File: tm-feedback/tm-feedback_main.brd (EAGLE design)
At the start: 100 x 80 mm, 24 parts

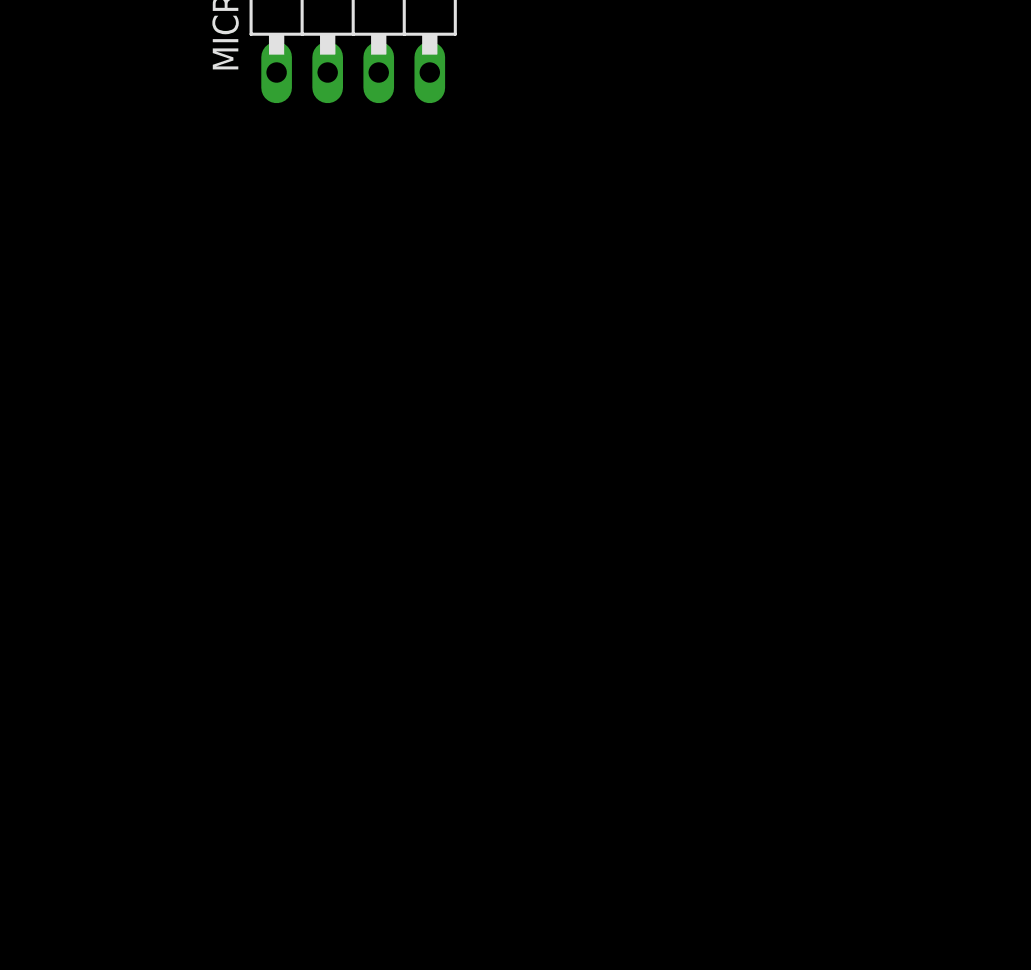
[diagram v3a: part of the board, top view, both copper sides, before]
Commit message: Add some custom library components to schematics
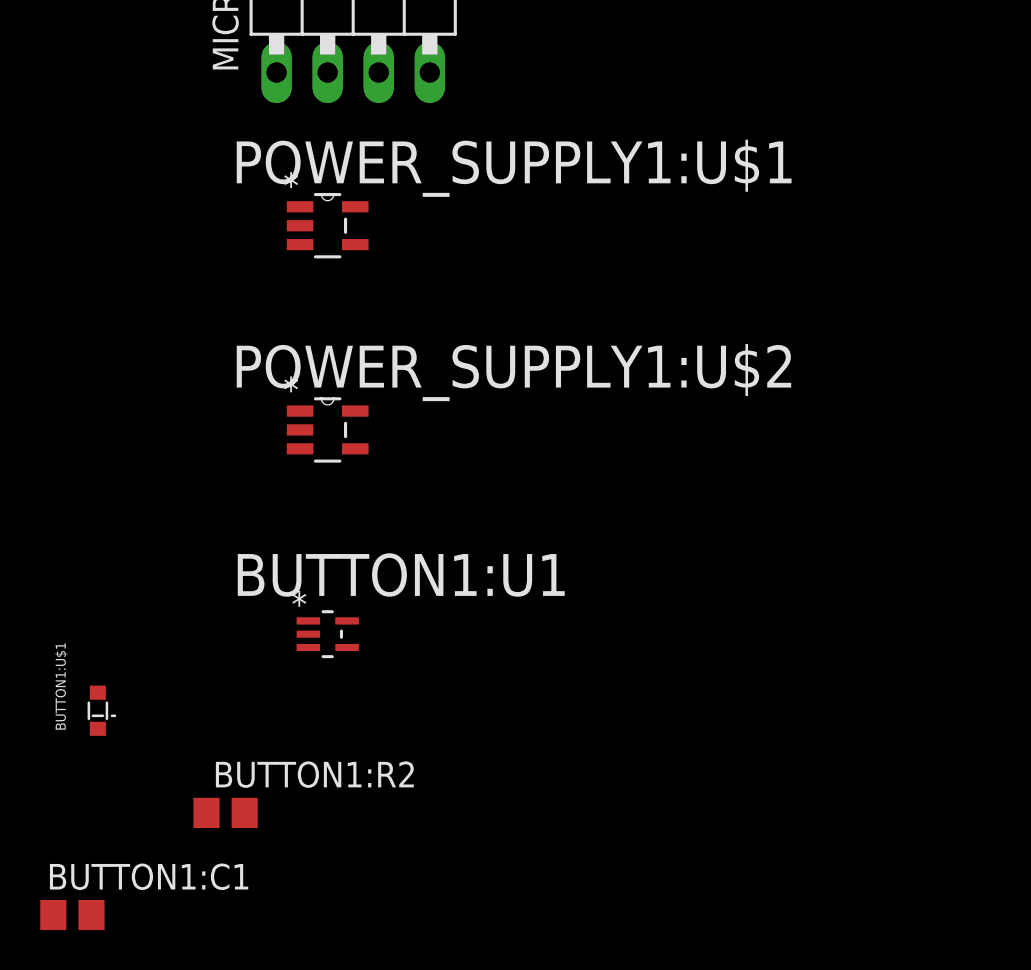
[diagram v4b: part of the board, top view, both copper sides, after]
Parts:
- added BUTTON1:C1: (no value), rcl:C0805
- added BUTTON1:R2: (no value), resistor:R0805
- added BUTTON1:U$1: DB2S308, tactile-music:SOD-523
- added BUTTON1:U1: 74AUP1G17GW, tactile-music:SOT65P212X110-5N
- added POWER_SUPPLY1:U$1, POWER_SUPPLY1:U$2: MCP1824T-3302E/OT, tactile-music:SOT95P270X145-5N
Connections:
- new net BUTTON1:VCC: BUTTON1:U1.5
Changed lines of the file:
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@@
 <element name="MICROCONTROLLER1:JP1" library="pinhead" package="1X06/90" value="" x="-54.61" y="-114.3"/>
 <element name="MICROCONTROLLER1:JP2" library="pinhead" package="1X04/90" value="" x="-57.15" y="-128.27"/>
+<element name="POWER_SUPPLY1:U$1" library="tactile-music" package="SOT95P270X145-5N" value="MCP1824T-3302E/OT" x="-58.42" y="-139.7">
+<attribute name="MPN" value="MCP1824T-3302E/OT" x="-58.42" y="-139.7" size="1.778" layer="27" display="off"/>
+<attribute name="SUPPLIER" value="Microchip" x="-58.42" y="-139.7" size="1.778" layer="27" display="off"/>
+<attribute name="OC_NEWARK" value="40M0704" x="-58.42" y="-139.7" size="1.778" layer="27" display="off"/>
+<attribute name="PACKAGE" value="SOT23-5" x="-58.42" y="-139.7" size="1.778" layer="27" display="off"/>
+<attribute name="OC_FARNELL" value="1578387" x="-58.42" y="-139.7" size="1.778" layer="27" display="off"/>
+</element>
+<element name="POWER_SUPPLY1:U$2" library="tactile-music" package="SOT95P270X145-5N" value="MCP1824T-3302E/OT" x="-58.42" y="-149.86">
+<attribute name="MPN" value="MCP1824T-3302E/OT" x="-58.42" y="-149.86" size="1.778" layer="27" display="off"/>
+<attribute name="SUPPLIER" value="Microchip" x="-58.42" y="-149.86" size="1.778" layer="27" display="off"/>
+<attribute name="OC_NEWARK" value="40M0704" x="-58.42" y="-149.86" size="1.778" layer="27" display="off"/>
+<attribute name="PACKAGE" value="SOT23-5" x="-58.42" y="-149.86" size="1.778" layer="27" display="off"/>
+<attribute name="OC_FARNELL" value="1578387" x="-58.42" y="-149.86" size="1.778" layer="27" display="off"/>
+</element>
+<element name="BUTTON1:U1" library="tactile-music" package="SOT65P212X110-5N" value="74AUP1G17GW" x="-58.42" y="-160.02">
+<attribute name="MPN" value="74AUP1G17GW " x="-58.42" y="-160.02" size="1.778" layer="27" display="off"/>
+<attribute name="SUPPLIER" value="NXP " x="-58.42" y="-160.02" size="1.778" layer="27" display="off"/>
+<attribute name="OC_NEWARK" value="55W4625 " x="-58.42" y="-160.02" size="1.778" layer="27" display="off"/>
+<attribute name="PACKAGE" value="TSSOP-5" x="-58.42" y="-160.02" size="1.778" layer="27" display="off"/>
+<attribute name="OC_FARNELL" value="2164682 " x="-58.42" y="-160.02" size="1.778" layer="27" display="off"/>
+</element>
+<element name="BUTTON1:R2" library="resistor" package="R0805" value="" x="-63.5" y="-168.91"/>
+<element name="BUTTON1:U$1" library="tactile-music" package="SOD-523" value="DB2S308" x="-69.85" y="-163.83"/>
+<element name="BUTTON1:C1" library="rcl" package="C0805" value="" x="-71.12" y="-173.99"/>
 </elements>
 <signals>
@@
 <wire x1="6.13" y1="-40.02" x2="3.49" y2="-53.34" width="0" layer="19" extent="1-1"/>
 </signal>
+<signal name="BUTTON1:VCC">
+<contactref element="BUTTON1:U1" pad="5"/>
+</signal>
 </signals>

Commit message: Made a start on the bluetooth module
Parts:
- added BLUETOOTH1:C1: (no value), rcl:C0805
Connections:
- removed net BLUETOOTH1:VDD: BLUETOOTH1:U$1.23
- new net D_3V3: BLUETOOTH1:C1.1, BLUETOOTH1:U$1.23
- net D_GND: now also BLUETOOTH1:C1.2
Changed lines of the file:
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@@
 <element name="BUTTON1:U$1" library="tactile-music" package="SOD-523" value="DB2S308" x="-69.85" y="-163.83"/>
 <element name="BUTTON1:C1" library="rcl" package="C0805" value="" x="-71.12" y="-173.99"/>
+<element name="BLUETOOTH1:C1" library="rcl" package="C0805" value="" x="-71.12" y="-179.07"/>
 </elements>
 <signals>
-<signal name="BLUETOOTH1:VDD">
-<contactref element="BLUETOOTH1:U$1" pad="23"/>
-</signal>
 <signal name="D_GND">
 <contactref element="BLUETOOTH1:U$1" pad="9"/>
 <contactref element="BLUETOOTH1:U$1" pad="16"/>
 <contactref element="BLUETOOTH1:U$1" pad="1"/>
+<contactref element="BLUETOOTH1:C1" pad="2"/>
 <contactref element="BLUETOOTH1:U$1" pad="24"/>
+<wire x1="1.87" y1="-21.18" x2="-70.17" y2="-179.07" width="0" layer="19" extent="1-1"/>
 <wire x1="1.87" y1="-10.28" x2="1.87" y2="-21.18" width="0" layer="19" extent="1-1"/>
 <wire x1="13.37" y1="-21.18" x2="1.87" y2="-21.18" width="0" layer="19" extent="1-1"/>
@@
 <contactref element="BUTTON1:U1" pad="5"/>
 </signal>
+<signal name="D_3V3">
+<contactref element="BLUETOOTH1:U$1" pad="23"/>
+<contactref element="BLUETOOTH1:C1" pad="1"/>
+<wire x1="13.37" y1="-11.48" x2="-72.07" y2="-179.07" width="0" layer="19" extent="1-1"/>
+</signal>
 </signals>

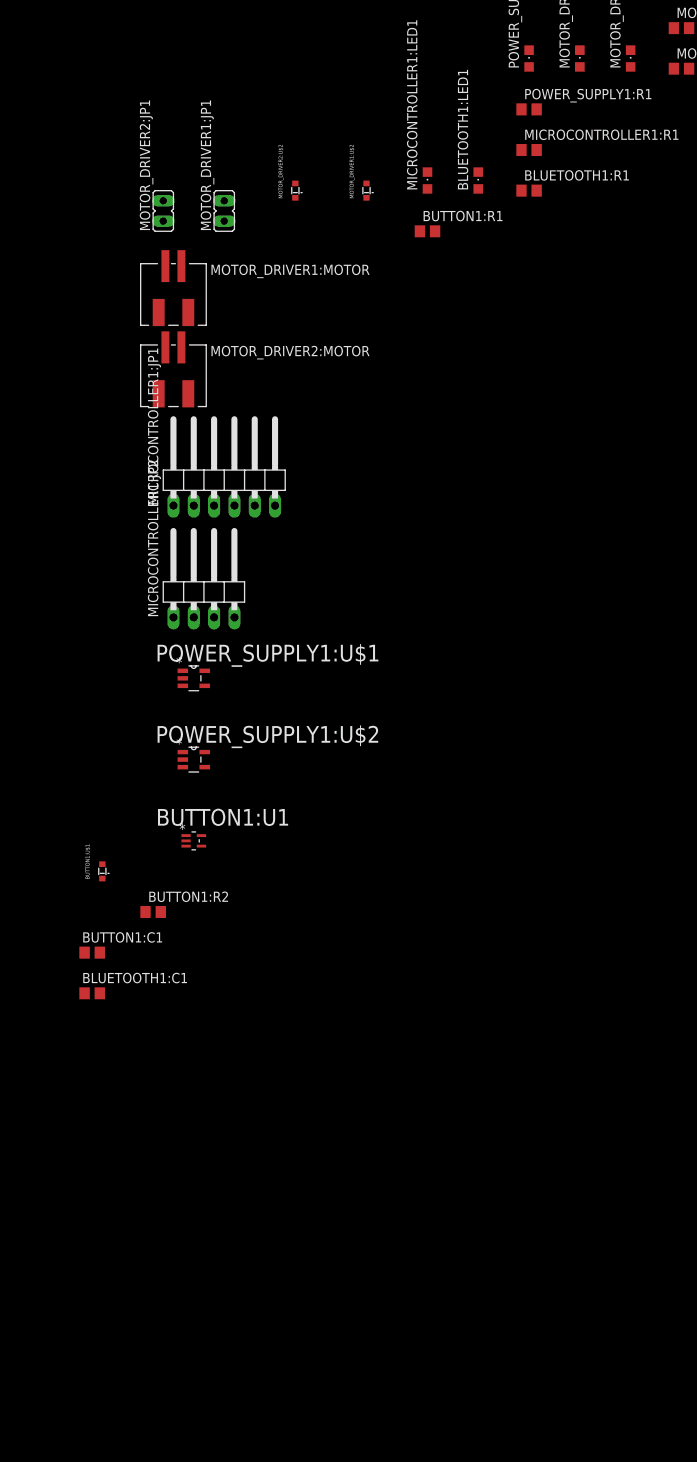
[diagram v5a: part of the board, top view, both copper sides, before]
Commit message: Completed Bluetooth Module
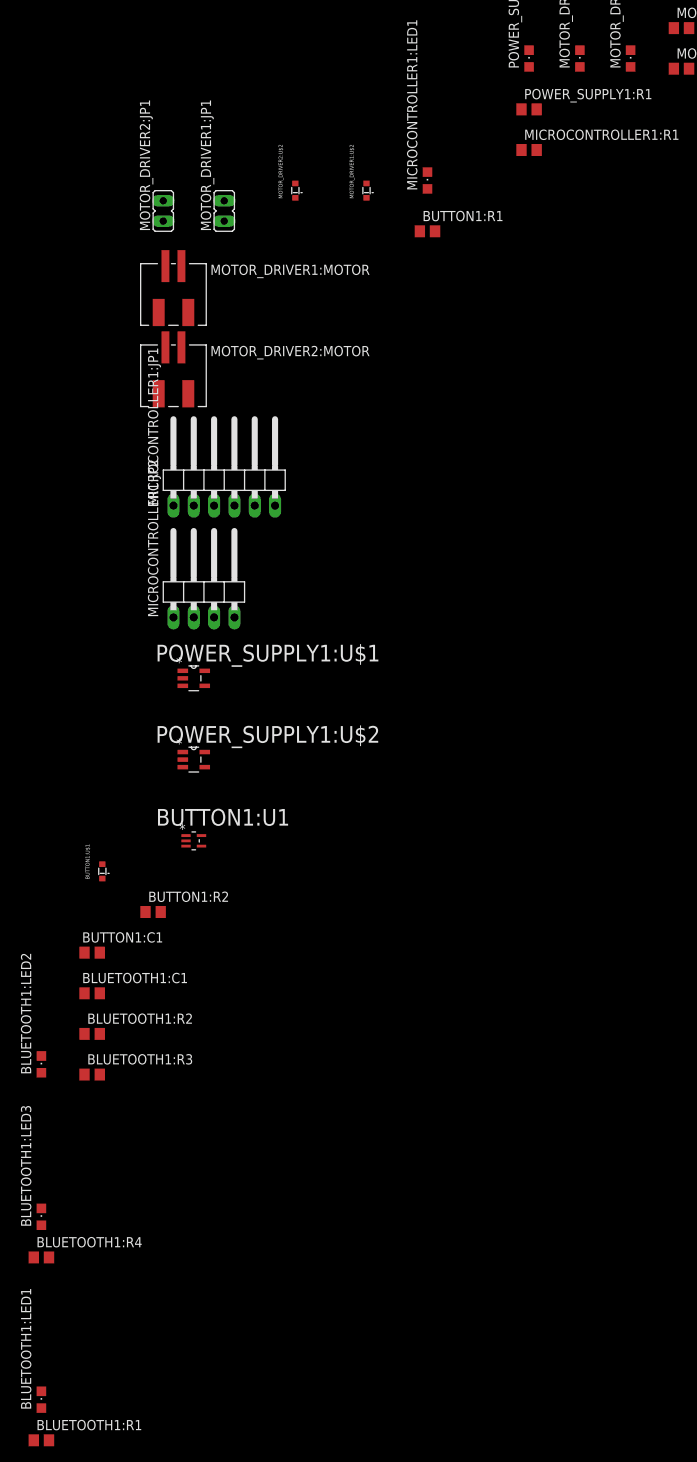
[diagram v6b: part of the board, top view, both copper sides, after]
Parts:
- added BLUETOOTH1:LED2, BLUETOOTH1:LED3: (no value), led:CHIPLED_0805
- added BLUETOOTH1:R2, BLUETOOTH1:R3, BLUETOOTH1:R4: (no value), resistor:R0805
- moved BLUETOOTH1:R1 167.7 mm to (-77.5, -234.9)
- moved BLUETOOTH1:LED1 161.9 mm to (-77.5, -229.9)
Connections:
- new net BLUETOOTH1:CMD/MLDP: BLUETOOTH1:U$1.8
- new net BLUETOOTH1:CONN: BLUETOOTH1:R3.2, BLUETOOTH1:U$1.10
- new net BLUETOOTH1:MLDP_EV: BLUETOOTH1:R4.2, BLUETOOTH1:U$1.11
- new net BLUETOOTH1:N$6: BLUETOOTH1:LED2.A, BLUETOOTH1:R3.1
- new net BLUETOOTH1:N$7: BLUETOOTH1:LED3.A, BLUETOOTH1:R4.1
- new net BLUETOOTH1:N$8: BLUETOOTH1:LED1.A, BLUETOOTH1:R1.1
- new net BLUETOOTH1:UART_CTS: BLUETOOTH1:U$1.14
- new net BLUETOOTH1:UART_RTS: BLUETOOTH1:U$1.18
- new net BLUETOOTH1:UART_RX: BLUETOOTH1:U$1.6
- new net BLUETOOTH1:WAKE_HW: BLUETOOTH1:U$1.15
- new net BLUETOOTH1:WAKE_SW: BLUETOOTH1:R2.2, BLUETOOTH1:U$1.7
- new net BLUETOOTH1:WS: BLUETOOTH1:R1.2, BLUETOOTH1:U$1.12
- new net N$2: BLUETOOTH1:U$1.5
- net D_GND: now also BLUETOOTH1:LED1.C, BLUETOOTH1:LED2.C, BLUETOOTH1:LED3.C, BLUETOOTH1:R2.1
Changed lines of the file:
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@@
 <element name="POWER_SUPPLY1:R1" library="resistor" package="R0805" value="" x="-16.51" y="-68.58"/>
 <element name="MICROCONTROLLER1:R1" library="resistor" package="R0805" value="" x="-16.51" y="-73.66"/>
-<element name="BLUETOOTH1:R1" library="resistor" package="R0805" value="" x="-16.51" y="-78.74"/>
-<element name="BLUETOOTH1:LED1" library="led" package="CHIPLED_0805" value="" x="-22.86" y="-77.47"/>
 <element name="MICROCONTROLLER1:LED1" library="led" package="CHIPLED_0805" value="" x="-29.21" y="-77.47"/>
 <element name="BUTTON1:R1" library="resistor" package="R0805" value="" x="-29.21" y="-83.82"/>
@@
 <element name="BUTTON1:C1" library="rcl" package="C0805" value="" x="-71.12" y="-173.99"/>
 <element name="BLUETOOTH1:C1" library="rcl" package="C0805" value="" x="-71.12" y="-179.07"/>
+<element name="BLUETOOTH1:R2" library="resistor" package="R0805" value="" x="-71.12" y="-184.15"/>
+<element name="BLUETOOTH1:R3" library="resistor" package="R0805" value="" x="-71.12" y="-189.23"/>
+<element name="BLUETOOTH1:LED2" library="led" package="CHIPLED_0805" value="" x="-77.47" y="-187.96"/>
+<element name="BLUETOOTH1:R4" library="resistor" package="R0805" value="" x="-77.47" y="-212.09"/>
+<element name="BLUETOOTH1:LED3" library="led" package="CHIPLED_0805" value="" x="-77.47" y="-207.01"/>
+<element name="BLUETOOTH1:R1" library="resistor" package="R0805" value="" x="-77.47" y="-234.95"/>
+<element name="BLUETOOTH1:LED1" library="led" package="CHIPLED_0805" value="" x="-77.47" y="-229.87"/>
 </elements>
 <signals>
@@
 <contactref element="BLUETOOTH1:C1" pad="2"/>
 <contactref element="BLUETOOTH1:U$1" pad="24"/>
+<contactref element="BLUETOOTH1:R2" pad="1"/>
+<contactref element="BLUETOOTH1:LED2" pad="C"/>
+<contactref element="BLUETOOTH1:LED3" pad="C"/>
+<contactref element="BLUETOOTH1:LED1" pad="C"/>
+<wire x1="-72.07" y1="-184.15" x2="-70.17" y2="-179.07" width="0" layer="19" extent="1-1"/>
+<wire x1="-77.47" y1="-186.91" x2="-72.07" y2="-184.15" width="0" layer="19" extent="1-1"/>
+<wire x1="-77.47" y1="-205.96" x2="-77.47" y2="-186.91" width="0" layer="19" extent="1-1"/>
+<wire x1="-77.47" y1="-228.82" x2="-77.47" y2="-205.96" width="0" layer="19" extent="1-1"/>
 <wire x1="1.87" y1="-21.18" x2="-70.17" y2="-179.07" width="0" layer="19" extent="1-1"/>
 <wire x1="1.87" y1="-10.28" x2="1.87" y2="-21.18" width="0" layer="19" extent="1-1"/>
@@
 <wire x1="13.37" y1="-11.48" x2="-72.07" y2="-179.07" width="0" layer="19" extent="1-1"/>
 </signal>
+<signal name="N$2">
+<contactref element="BLUETOOTH1:U$1" pad="5"/>
+</signal>
+<signal name="BLUETOOTH1:UART_RX">
+<contactref element="BLUETOOTH1:U$1" pad="6"/>
+</signal>
+<signal name="BLUETOOTH1:WAKE_SW">
+<contactref element="BLUETOOTH1:U$1" pad="7"/>
+<contactref element="BLUETOOTH1:R2" pad="2"/>
+<wire x1="1.87" y1="-17.48" x2="-70.17" y2="-184.15" width="0" layer="19" extent="1-1"/>
+</signal>
+<signal name="BLUETOOTH1:UART_RTS">
+<contactref element="BLUETOOTH1:U$1" pad="18"/>
+</signal>
+<signal name="BLUETOOTH1:CMD/MLDP">
+<contactref element="BLUETOOTH1:U$1" pad="8"/>
+</signal>
+<signal name="BLUETOOTH1:N$6">
+<contactref element="BLUETOOTH1:R3" pad="1"/>
+<contactref element="BLUETOOTH1:LED2" pad="A"/>
+<wire x1="-72.07" y1="-189.23" x2="-77.47" y2="-189.01" width="0" layer="19" extent="1-1"/>
+</signal>
+<signal name="BLUETOOTH1:N$7">
+<contactref element="BLUETOOTH1:R4" pad="1"/>
+<contactref element="BLUETOOTH1:LED3" pad="A"/>
+<wire x1="-77.47" y1="-208.06" x2="-78.42" y2="-212.09" width="0" layer="19" extent="1-1"/>
+</signal>
+<signal name="BLUETOOTH1:N$8">
+<contactref element="BLUETOOTH1:R1" pad="1"/>
+<contactref element="BLUETOOTH1:LED1" pad="A"/>
+<wire x1="-77.47" y1="-230.92" x2="-78.42" y2="-234.95" width="0" layer="19" extent="1-1"/>
+</signal>
+<signal name="BLUETOOTH1:CONN">
+<contactref element="BLUETOOTH1:U$1" pad="10"/>
+<contactref element="BLUETOOTH1:R3" pad="2"/>
+<wire x1="-70.17" y1="-189.23" x2="4.62" y2="-21.18" width="0" layer="19" extent="1-1"/>
+</signal>
+<signal name="BLUETOOTH1:MLDP_EV">
+<contactref element="BLUETOOTH1:U$1" pad="11"/>
+<contactref element="BLUETOOTH1:R4" pad="2"/>
+<wire x1="5.82" y1="-21.18" x2="-76.52" y2="-212.09" width="0" layer="19" extent="1-1"/>
+</signal>
+<signal name="BLUETOOTH1:WS">
+<contactref element="BLUETOOTH1:U$1" pad="12"/>
+<contactref element="BLUETOOTH1:R1" pad="2"/>
+<wire x1="7.02" y1="-21.18" x2="-76.52" y2="-234.95" width="0" layer="19" extent="1-1"/>
+</signal>
+<signal name="BLUETOOTH1:UART_CTS">
+<contactref element="BLUETOOTH1:U$1" pad="14"/>
+</signal>
+<signal name="BLUETOOTH1:WAKE_HW">
+<contactref element="BLUETOOTH1:U$1" pad="15"/>
+</signal>
 </signals>

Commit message: Added value to bluetooth module decoupling cap
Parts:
- BLUETOOTH1:C1: value (none) -> 4.7uF
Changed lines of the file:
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@@
 <element name="BUTTON1:U$1" library="tactile-music" package="SOD-523" value="DB2S308" x="-69.85" y="-163.83"/>
 <element name="BUTTON1:C1" library="rcl" package="C0805" value="" x="-71.12" y="-173.99"/>
-<element name="BLUETOOTH1:C1" library="rcl" package="C0805" value="" x="-71.12" y="-179.07"/>
+<element name="BLUETOOTH1:C1" library="rcl" package="C0805" value="4.7uF" x="-71.12" y="-179.07"/>
 <element name="BLUETOOTH1:R2" library="resistor" package="R0805" value="" x="-71.12" y="-184.15"/>
 <element name="BLUETOOTH1:R3" library="resistor" package="R0805" value="" x="-71.12" y="-189.23"/>
@@
 <contactref element="BLUETOOTH1:U$1" pad="1"/>
 <contactref element="BLUETOOTH1:C1" pad="2"/>
-<contactref element="BLUETOOTH1:U$1" pad="24"/>
 <contactref element="BLUETOOTH1:R2" pad="1"/>
 <contactref element="BLUETOOTH1:LED2" pad="C"/>
 <contactref element="BLUETOOTH1:LED3" pad="C"/>
 <contactref element="BLUETOOTH1:LED1" pad="C"/>
+<contactref element="BLUETOOTH1:U$1" pad="24"/>
 <wire x1="-72.07" y1="-184.15" x2="-70.17" y2="-179.07" width="0" layer="19" extent="1-1"/>
 <wire x1="-77.47" y1="-186.91" x2="-72.07" y2="-184.15" width="0" layer="19" extent="1-1"/>
